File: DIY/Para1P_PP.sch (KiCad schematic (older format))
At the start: 5 parts, among them J1 Atari_SEGA_DE9, J3 DB25_Male, U1 74AHCT125N, U2 74AHCT125N, U3 74AHCT125N

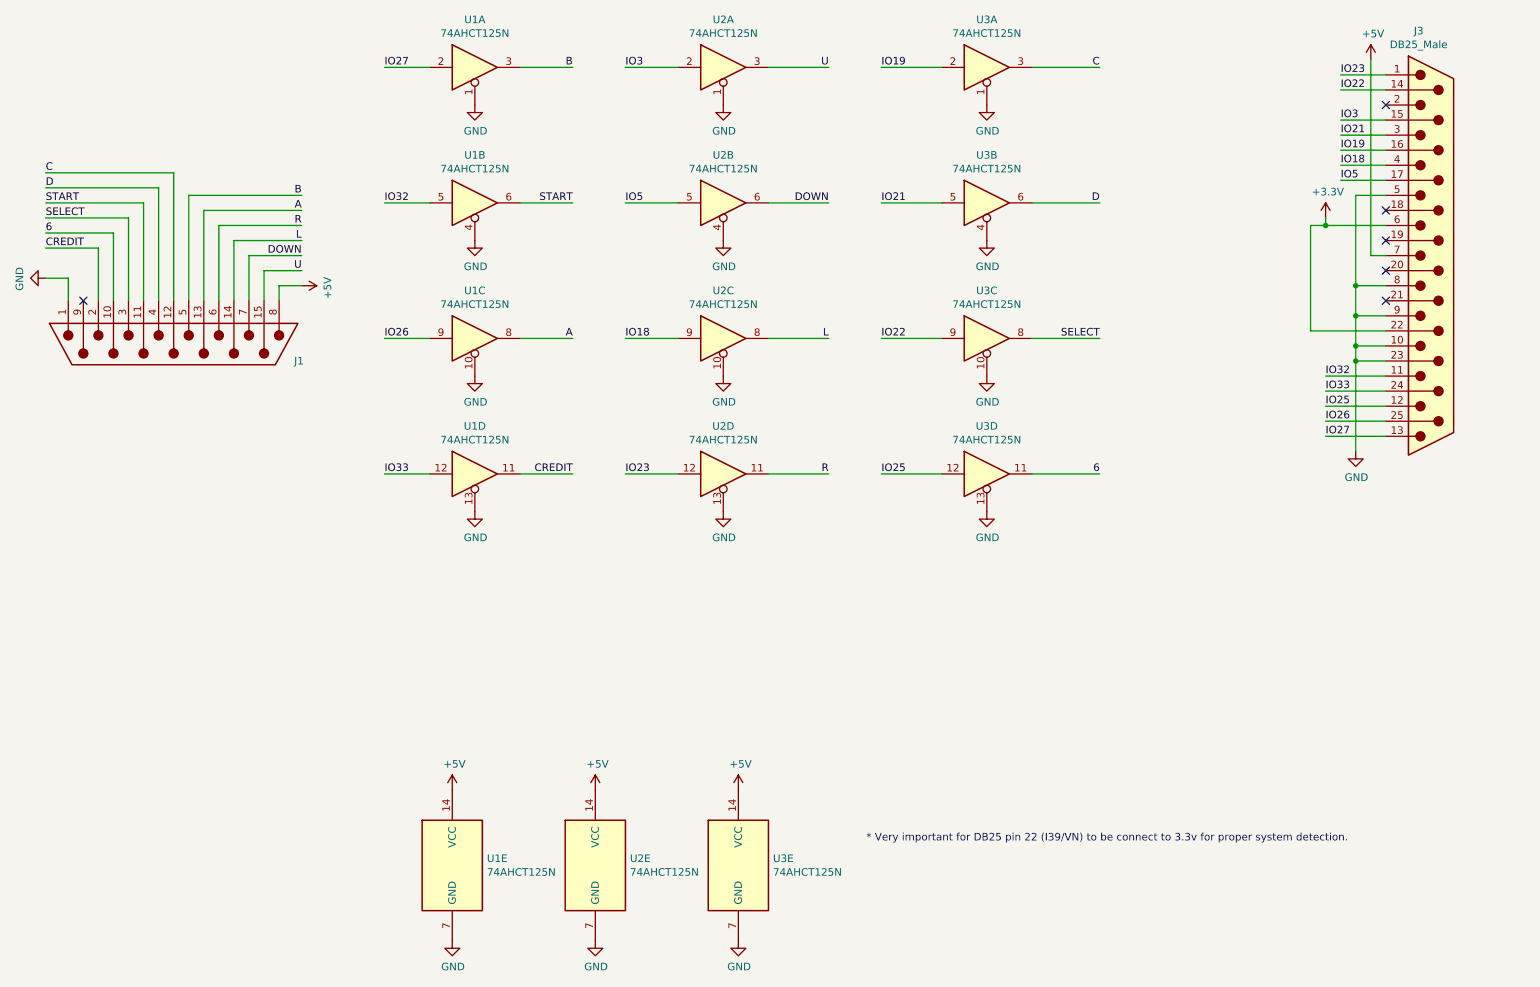
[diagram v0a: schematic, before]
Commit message: Simplify parallel schematics
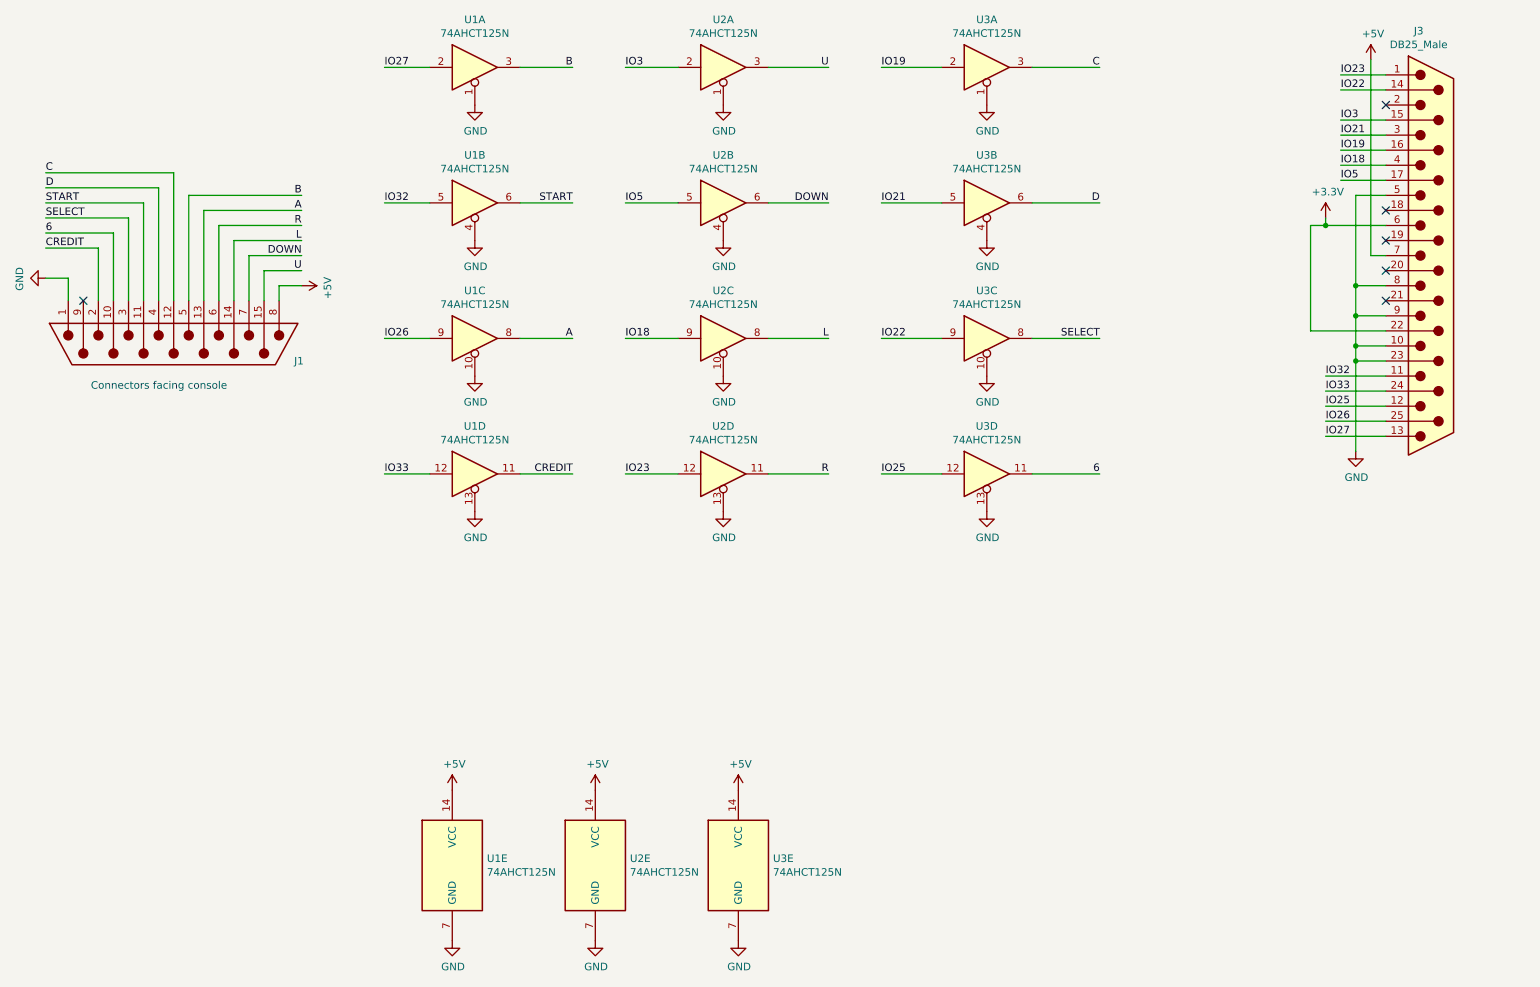
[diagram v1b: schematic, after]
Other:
- note added: "Connectors facing console"
- note removed: "* Very important for DB25 pin 22 (I39/VN) to be connect to 3.3v for proper system detection."
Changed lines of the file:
@@
 $Descr USLetter 11000 8500
 encoding utf-8
-Sheet 10 19
+Sheet 10 20
 Title "BlueRetro - Parallel 1P Push-Pull adapter cable"
 Date "2022-01-30"
 Rev "v1.1"
-Comp "©2020 Jacques Gagnon, licensed under CC-BY-4.0"
+Comp "©2020-2022 Jacques Gagnon, licensed under CC-BY-4.0"
 Comment1 ""
 Comment2 ""
@@
 	1    0    0    -1
 $EndComp
-Text Notes 6350 6900 0    50   ~ 0
-* Very important for DB25 pin 22 (I39/VN) to be connect to 3.3v for proper system detection.
 $Comp
 L power:GND #PWR?
@@
 Text Label 2600 3100 2    50   ~ 0
 U
+Text Notes 1200 3900 0    50   ~ 0
+Connectors facing console
 $EndSCHEMATC
